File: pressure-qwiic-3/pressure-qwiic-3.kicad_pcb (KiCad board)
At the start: 2 copper layers, 40 x 17 mm, 14 parts, among them IC1 SC18IS606PWJ, J1 Conn_01x04_Male, J2 Conn_01x04_Male, J3 Conn_01x04_Male, U1 TruStability_SPI, U2 TruStability_SPI, U3 TruStability_SPI

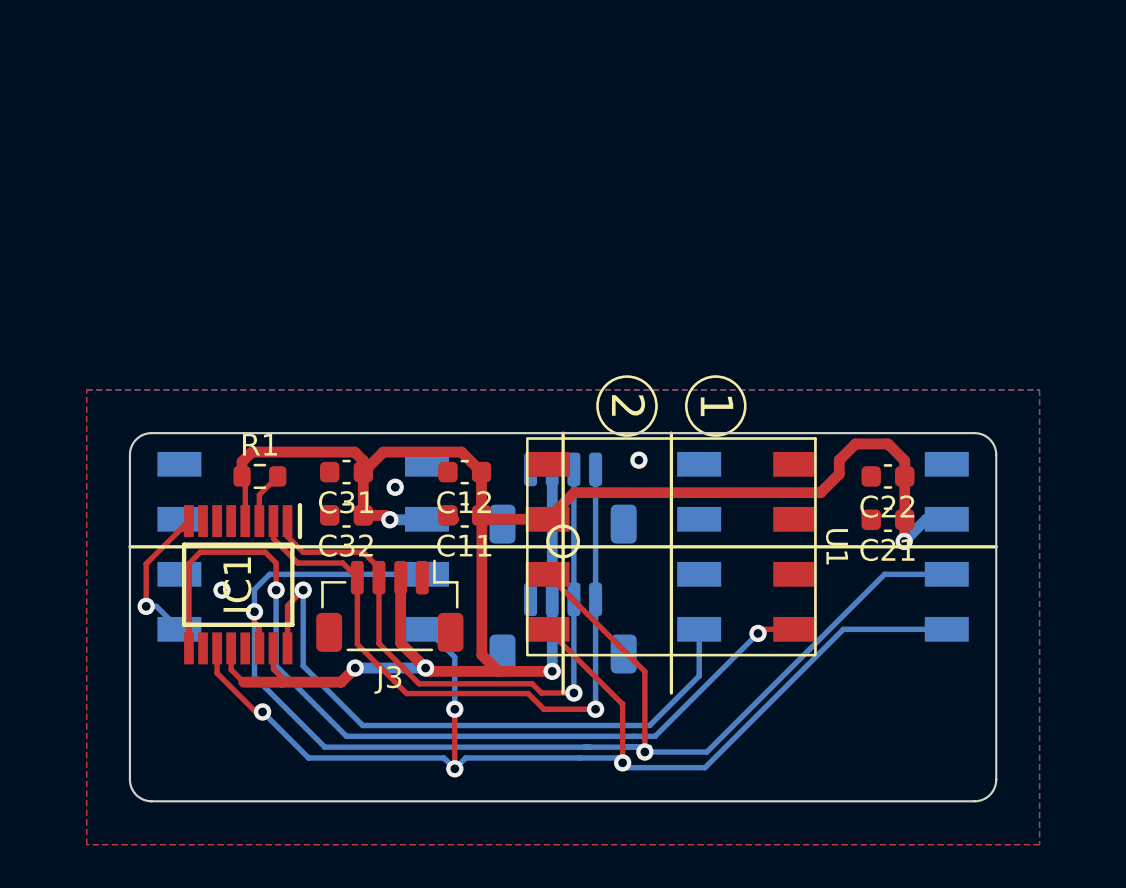
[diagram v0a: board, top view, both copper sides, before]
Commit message: Fixed QWIIC pinouts. Added QWIIC logo.
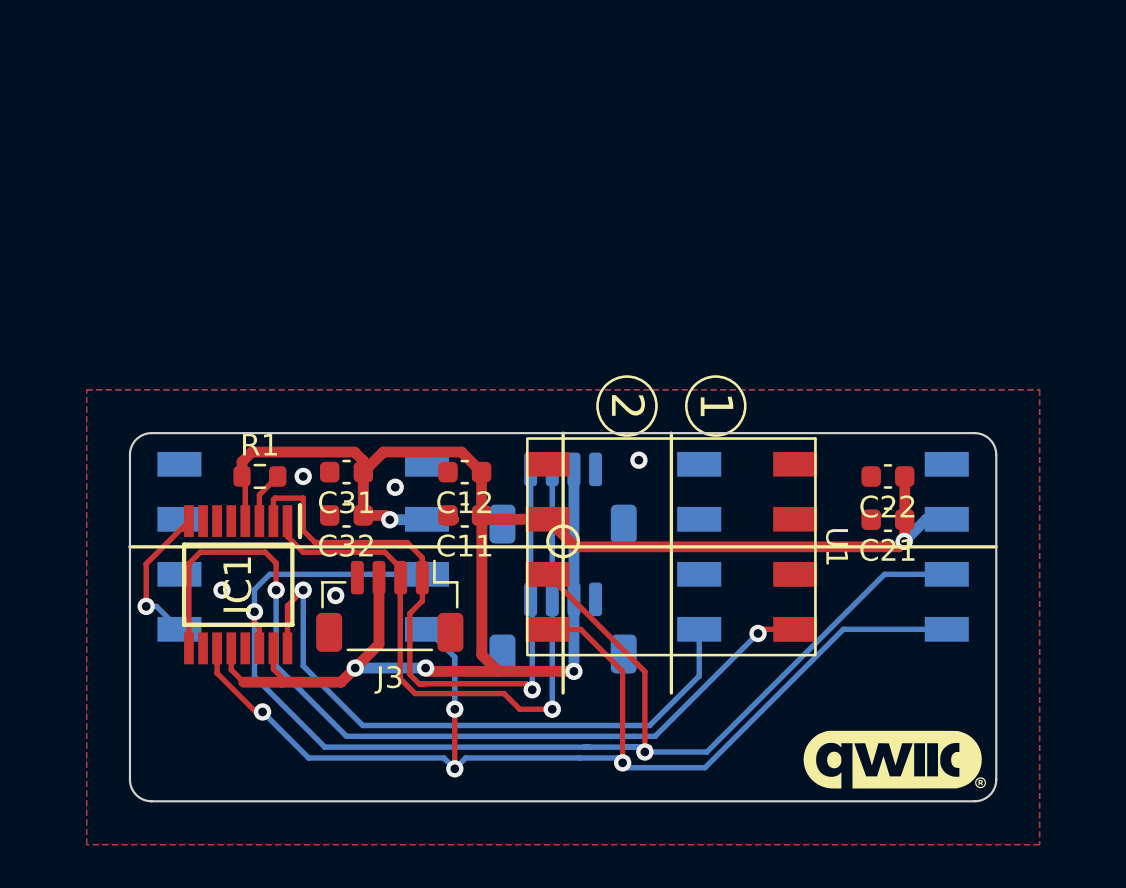
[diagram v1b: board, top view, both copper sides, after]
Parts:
- added G***: LOGO, airball-hardware:qwiic-logo, F.Cu at (15.2, 15.0)
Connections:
- J1 pad 1: GND -> /SCL
- J1 pad 2: +3V3 -> /SDA
- J1 pad 3: /SDA -> +3V3
- J1 pad 4: /SCL -> GND
- J2 pad 1: GND -> /SCL
- J2 pad 2: +3V3 -> /SDA
- J2 pad 3: /SDA -> +3V3
- J2 pad 4: /SCL -> GND
- J3 pad 1: GND -> /SCL
- J3 pad 2: +3V3 -> /SDA
- J3 pad 3: /SDA -> +3V3
- J3 pad 4: /SCL -> GND
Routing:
- net /SDA: track 29.1 -> 30.1 mm
- net /SCL: track 31.0 -> 31.9 mm
- net /SCLK: track 54.3 -> 55.2 mm
- net +3V3: track 89.9 -> 89.1 mm
- net GND: vias 3 -> 5

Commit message: Latest changes.
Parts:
- moved U2 2.00 mm to (14.0, 5.25)
- moved U3 2.00 mm to (-14.0, 5.25)
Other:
- board size 40 x 17 mm -> 45 x 17 mm
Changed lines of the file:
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@@
   )
   (footprint "airball-hardware:TruStability SMT" (layer "B.Cu")
-    (at 12 5.25 -90)
+    (at 14 5.25 -90)
     (property "Sheetfile" "pressure-qwiic-3.kicad_sch")
     (property "Sheetname" "")
@@
   )
   (footprint "airball-hardware:TruStability SMT" (layer "B.Cu")
-    (at -12 5.25 -90)
+    (at -14 5.25 -90)
     (property "Sheetfile" "pressure-qwiic-3.kicad_sch")
     (property "Sheetname" "")
@@
   (gr_line (start 5 0) (end 5 12) (layer "F.SilkS") (width 0.15))
   (gr_line (start -20 5.25) (end 20 5.25) (layer "F.SilkS") (width 0.15))
-  (gr_arc (start -20 1) (mid -19.707107 0.292893) (end -19 0) (layer "Edge.Cuts") (width 0.1))
-  (gr_line (start 20 1) (end 20 16) (layer "Edge.Cuts") (width 0.1))
-  (gr_line (start 19 17) (end -19 17) (layer "Edge.Cuts") (width 0.1))
-  (gr_arc (start 19 0) (mid 19.707107 0.292893) (end 20 1) (layer "Edge.Cuts") (width 0.1))
-  (gr_line (start -19 0) (end 19 0) (layer "Edge.Cuts") (width 0.1))
-  (gr_line (start -20 16) (end -20 1) (layer "Edge.Cuts") (width 0.1))
-  (gr_arc (start 20 16) (mid 19.707107 16.707107) (end 19 17) (layer "Edge.Cuts") (width 0.1))
-  (gr_arc (start -19 17) (mid -19.707107 16.707107) (end -20 16) (layer "Edge.Cuts") (width 0.1))
+  (gr_arc (start -22.5 1) (mid -22.207107 0.292893) (end -21.5 0) (layer "Edge.Cuts") (width 0.1))
+  (gr_line (start 22.5 1) (end 22.5 16) (layer "Edge.Cuts") (width 0.1))
+  (gr_line (start 21.5 17) (end -21.5 17) (layer "Edge.Cuts") (width 0.1))
+  (gr_arc (start 21.5 0) (mid 22.207107 0.292893) (end 22.5 1) (layer "Edge.Cuts") (width 0.1))
+  (gr_line (start -21.5 0) (end 21.5 0) (layer "Edge.Cuts") (width 0.1))
+  (gr_line (start -22.5 16) (end -22.5 1) (layer "Edge.Cuts") (width 0.1))
+  (gr_arc (start 22.5 16) (mid 22.207107 16.707107) (end 21.5 17) (layer "Edge.Cuts") (width 0.1))
+  (gr_arc (start -21.5 17) (mid -22.207107 16.707107) (end -22.5 16) (layer "Edge.Cuts") (width 0.1))
   (segment (start -3.58558 3.98) (end -3.75 4.14442) (width 0.5) (layer "F.Cu") (net 1))
   (segment (start -13.375 10.9005) (end -13 11.2755) (width 0.25) (layer "F.Cu") (net 1))
@@
     (connect_pads (clearance 0.15))
     (min_thickness 0.254) (filled_areas_thickness no)
-    (fill yes (thermal_gap 0.15) (thermal_bridge_width 0.508))
+    (fill (thermal_gap 0.15) (thermal_bridge_width 0.508))
     (polygon
       (pts
-        (xy 22 19)
-        (xy -22 19)
-        (xy -22 -2)
-        (xy 22 -2)
+        (xy 24 19)
+        (xy -24 19)
+        (xy -24 -2)
+        (xy 24 -2)
       )
     )

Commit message: Almost complete.
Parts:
- added J4: Conn_01x04_Male, airball-hardware:JST_SH_BM04B-SRSS-TB_1x04-1MP_P1.00mm_Vertical, F.Cu at (13.0, 14.0)
- C21, C22, C31, C32, IC1, R1: moved to B.Cu
- moved R1 17.4 mm to (1.00, 10.8)
- moved J1 17.0 mm to (13.0, 14.0), turned to 180 degrees
- moved G*** 15.2 mm to (0.00, 15.0)
- moved IC1 15.1 mm to (0.00, 5.00), turned to 90 degrees
- moved J2 13.9 mm to (-13.0, 14.0), turned to 180 degrees
- moved C11 10.2 mm to (5.50, 5.50), turned to -90 degrees
- moved C12 10.1 mm to (5.50, 2.50), turned to 90 degrees
- moved U1 8.00 mm to (13.0, 5.25)
- moved J3 7.81 mm to (-13.0, 14.0)
- moved C31 5.83 mm to (-5.50, 5.50), turned to -90 degrees
- moved C21 5.65 mm to (20.5, 5.28), turned to -90 degrees
- moved C22 5.51 mm to (20.5, 2.27), turned to 90 degrees
- moved C32 4.68 mm to (-5.50, 2.50), turned to 90 degrees
- moved U2 1.00 mm to (13.0, 5.25)
- moved U3 1.00 mm to (-13.0, 5.25)
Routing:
- net /MISO: track 62.6 -> 38.8 mm, vias 2 -> 3
- net /!CS1: track 29.0 -> 11.0 mm, vias 1 -> 2
- net /SDA: track 30.1 -> 43.4 mm, vias 1 -> 5
- net /SCLK: track 55.2 -> 43.5 mm, vias 4 -> 5
- net /!CS0: track 40.5 -> 29.8 mm, vias 2 -> 3
- net /SCL: track 31.9 -> 42.4 mm, vias 1 -> 3
- net /!CS2: track 6.73 -> 16.9 mm, vias 1 -> 0
- net Net-(IC1-Pad3): track 2.41 -> 3.16 mm
- net +3V3: track 89.1 -> 88.6 mm, vias 5 -> 4
- net GND: track 0.25 -> 0.00 mm, vias 5 -> 2

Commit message: More changes. Should be ready now.
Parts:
- added C1: 0.1uF, Capacitor_SMD:C_0603_1608Metric, B.Cu at (-2.00, 10.8)
- added G***: LOGO, airball-hardware:airball-logo-5mm, F.Cu at (-16.0, 3.00)
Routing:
- net +3V3: track 88.6 -> 90.0 mm, vias 4 -> 6
- net /SCLK: track 43.5 -> 44.1 mm
- net GND: vias 2 -> 0
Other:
- board text added: "Airball pressure sensor Copyright (C) 2023, The Airball Authors 2023-03-03"

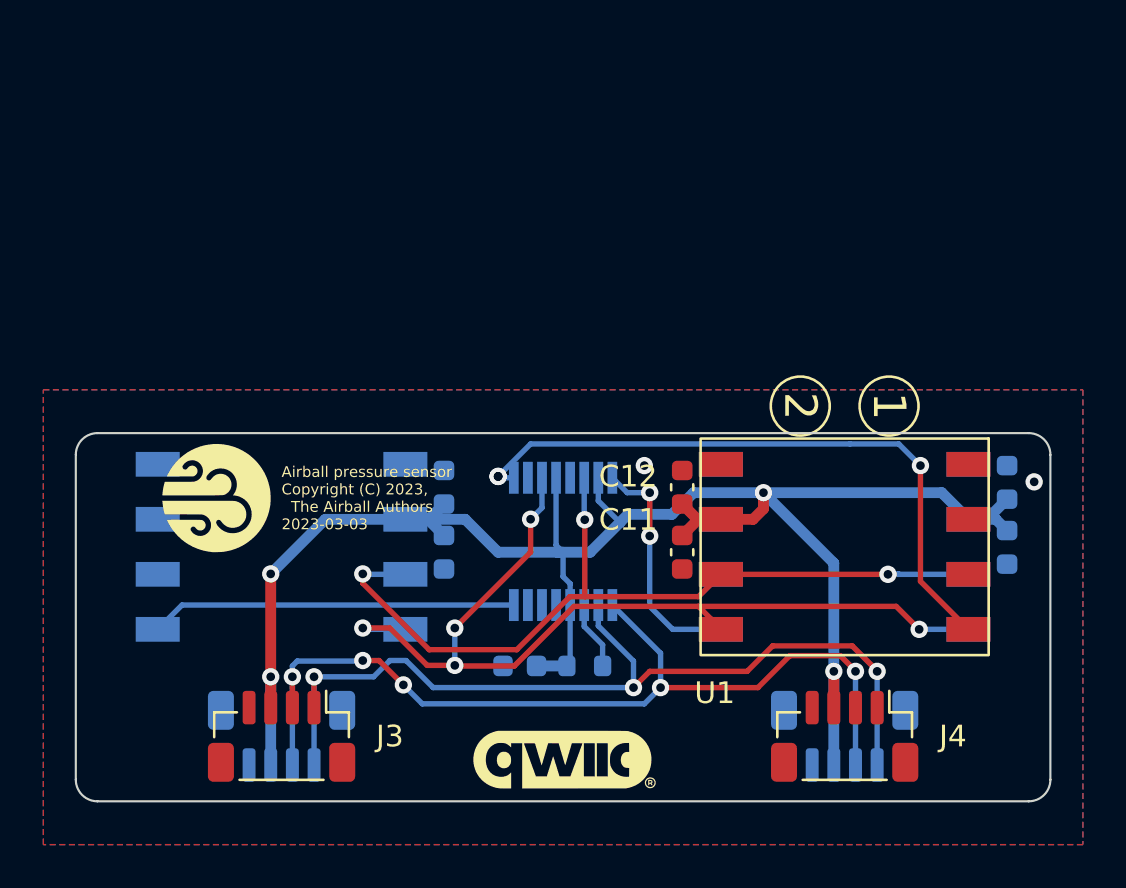
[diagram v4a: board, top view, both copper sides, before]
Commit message: Completed pressure-qwiic-3. Completed baro-temp-qwiic. Deleted baro-qwiic.
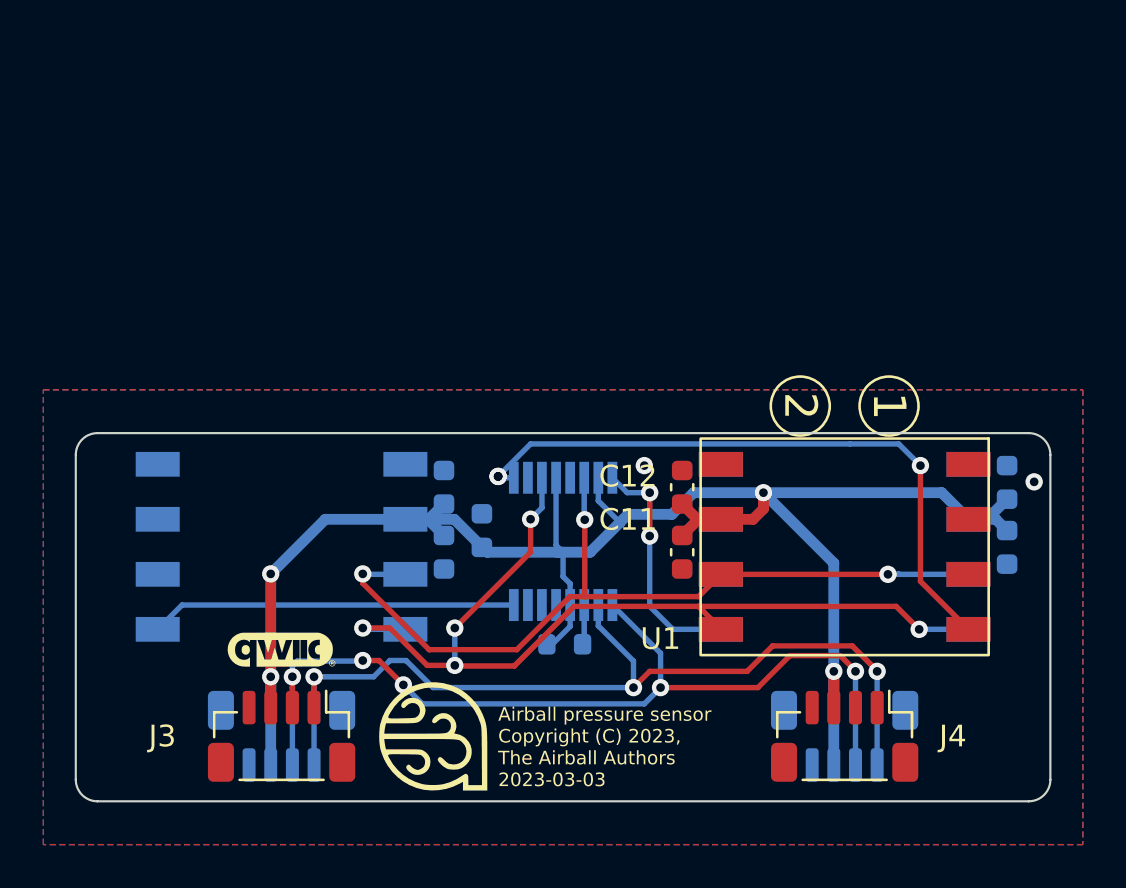
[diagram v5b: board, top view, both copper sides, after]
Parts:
- removed the G*** at (0.00, 15.0)
- added G***: LOGO, airball-hardware:qwiic-logo-5mm, F.Cu at (-13.0, 10.0)
- moved G*** 14.9 mm to (-6.00, 14.0)
- moved C1 6.49 mm to (-3.75, 4.50), turned to 90 degrees
- moved R1 1.36 mm to (0.07, 9.75)
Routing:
- net +3V3: track 90.0 -> 88.1 mm
- net Net-(IC1-Pad3): track 3.16 -> 1.84 mm

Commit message: Moved to 4 layer PCB and shrank the size. Re-routed.
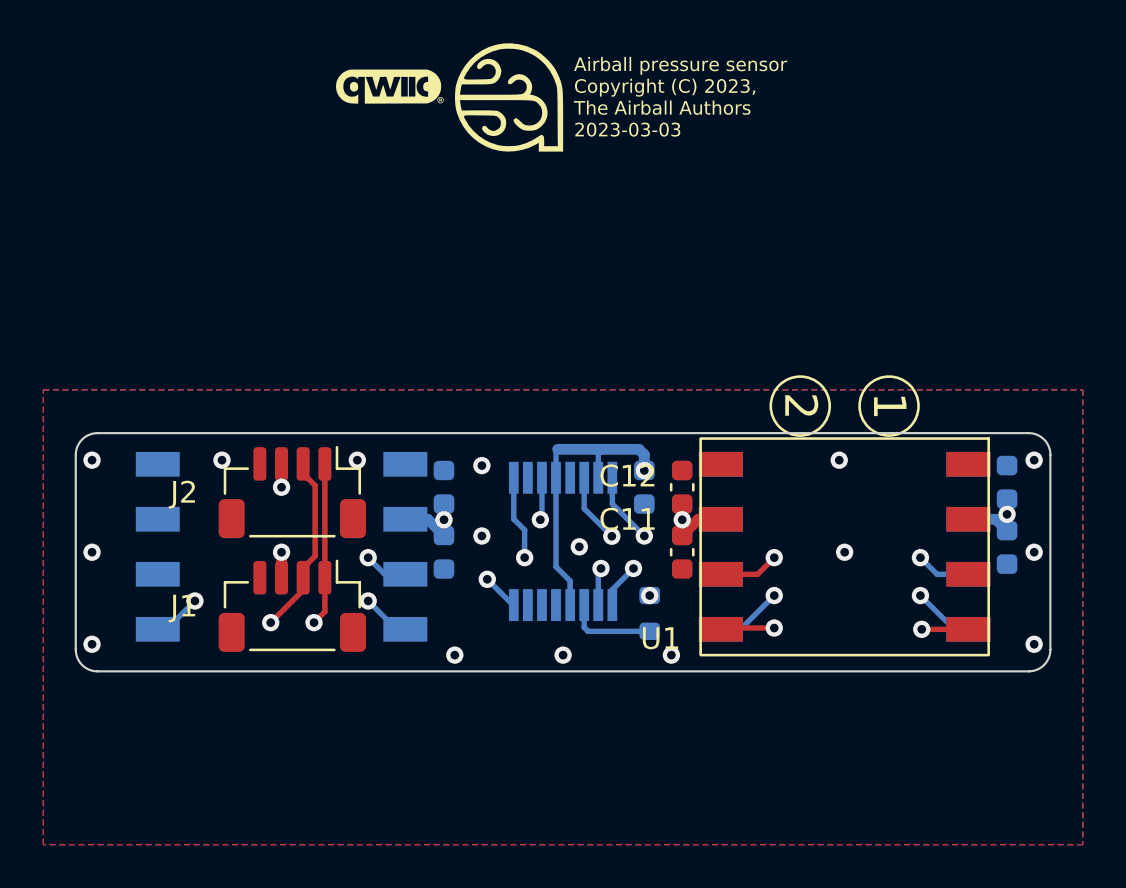
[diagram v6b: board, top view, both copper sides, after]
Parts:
- removed J3, J4: Conn_01x04_Male, airball-hardware:JST_SH_BM04B-SRSS-TB_1x04-1MP_P1.00mm_Vertical
- J1, J2: moved to F.Cu
- moved G*** 29.7 mm to (-2.50, -15.5)
- moved G*** 26.5 mm to (-8.00, -16.0)
- moved J1 26.2 mm to (-12.5, 8.00)
- moved J2 11.3 mm to (-12.5, 2.75)
- moved C1 7.76 mm to (3.75, 2.50), turned to -90 degrees
- moved R1 4.18 mm to (4.00, 8.32), turned to -90 degrees
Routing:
- net +3V3: track 88.1 -> 26.5 mm, vias 6 -> 7
- net /SCL: track 42.4 -> 24.1 mm, vias 3 -> 2
- net /SDA: track 43.4 -> 28.9 mm, vias 5 -> 2
- net /MISO: track 39.1 -> 44.5 mm, vias 3 -> 4
- net /!CS0: track 29.8 -> 25.9 mm, vias 3 -> 2
- net /!CS1: track 11.0 -> 13.6 mm
- net Net-(IC1-Pad3): track 1.84 -> 4.13 mm
- net /!CS2: track 16.9 -> 17.9 mm, vias 0 -> 2
- net /SCLK: track 44.1 -> 44.6 mm, vias 5 -> 4
- net GND: vias 0 -> 16
- added copper zone on In1.Cu, net +3V3
- added copper zone on In2.Cu, net +3V3
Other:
- board size 45 x 17 mm -> 45 x 11 mm
- copper layers 2 -> 4
